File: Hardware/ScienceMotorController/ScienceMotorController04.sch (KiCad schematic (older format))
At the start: 12 parts

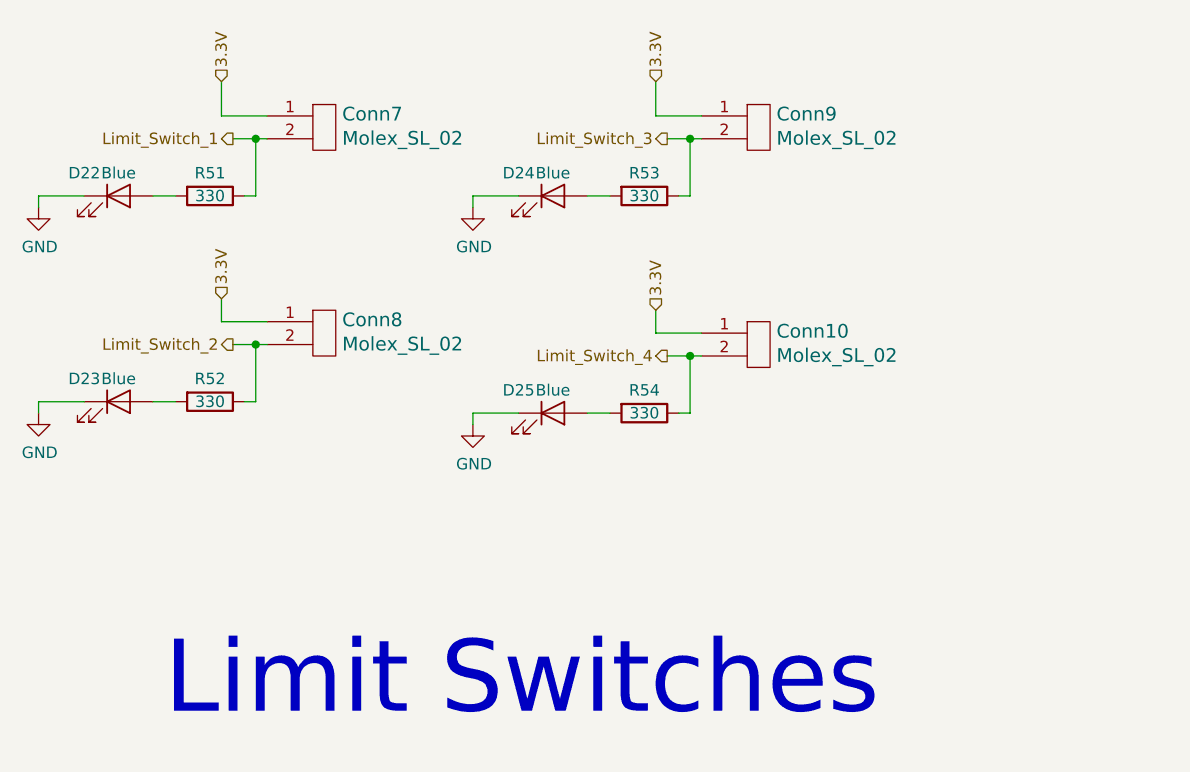
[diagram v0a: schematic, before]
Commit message: assigned most of the footprints
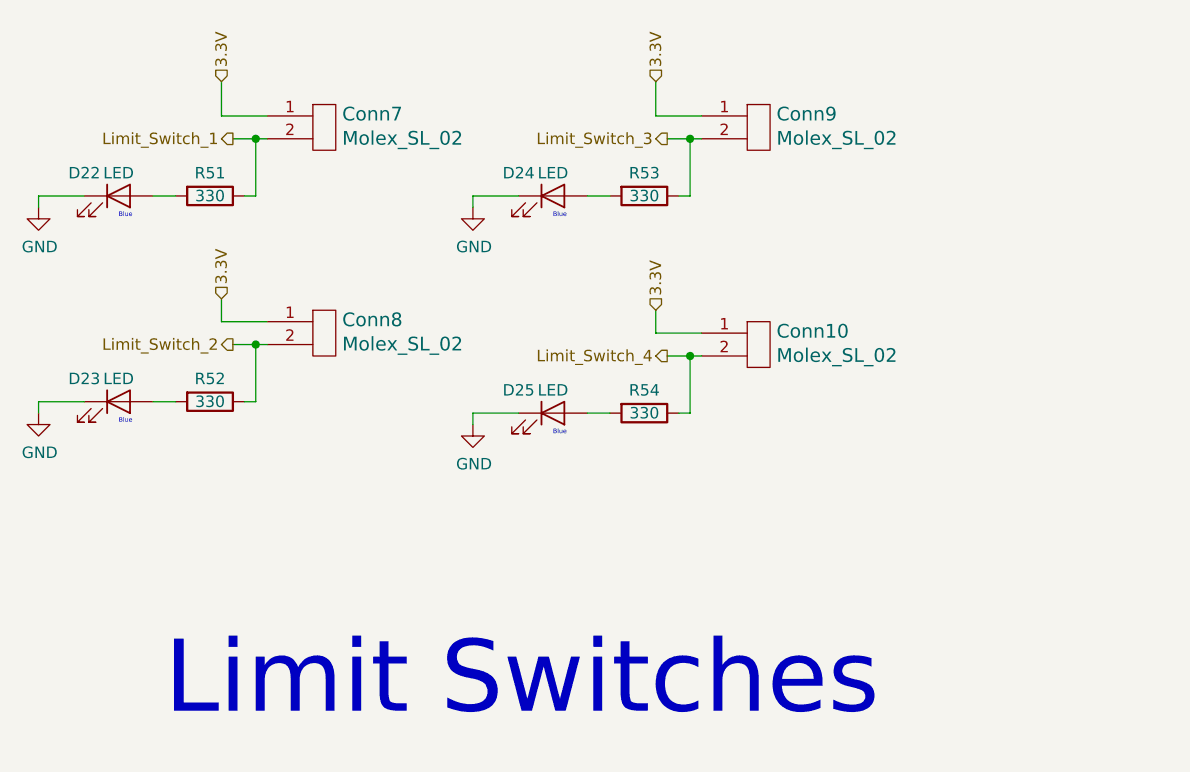
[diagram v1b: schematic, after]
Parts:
- Conn10, Conn7, Conn8, Conn9: footprint (none) -> MRDT_Connectors:MOLEX_SL_02_Vertical
- D22, D23, D24, D25: value Blue -> LED; footprint (none) -> LED_SMD:LED_0603_1608Metric_Pad1.05x0.95mm_HandSolder
- R51, R52, R53, R54: footprint (none) -> Resistor_SMD:R_0603_1608Metric_Pad1.05x0.95mm_HandSolder
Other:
- note added: "Blue"
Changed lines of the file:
@@
 F 0 "Conn7" H 8178 4658 60  0000 L CNN
 F 1 "Molex_SL_02" H 8178 4552 60  0000 L CNN
-F 2 "" H 8050 4400 60  0001 C CNN
+F 2 "MRDT_Connectors:MOLEX_SL_02_Vertical" H 8050 4400 60  0001 C CNN
 F 3 "" H 8050 4400 60  0001 C CNN
 	1    8050 4500
@@
 F 0 "Conn9" H 10078 4658 60  0000 L CNN
 F 1 "Molex_SL_02" H 10078 4552 60  0000 L CNN
-F 2 "" H 9950 4400 60  0001 C CNN
+F 2 "MRDT_Connectors:MOLEX_SL_02_Vertical" H 9950 4400 60  0001 C CNN
 F 3 "" H 9950 4400 60  0001 C CNN
 	1    9950 4500
@@
 F 0 "Conn8" H 8178 5558 60  0000 L CNN
 F 1 "Molex_SL_02" H 8178 5452 60  0000 L CNN
-F 2 "" H 8050 5300 60  0001 C CNN
+F 2 "MRDT_Connectors:MOLEX_SL_02_Vertical" H 8050 5300 60  0001 C CNN
 F 3 "" H 8050 5300 60  0001 C CNN
 	1    8050 5400
@@
 F 0 "Conn10" H 10078 5608 60  0000 L CNN
 F 1 "Molex_SL_02" H 10078 5502 60  0000 L CNN
-F 2 "" H 9950 5350 60  0001 C CNN
+F 2 "MRDT_Connectors:MOLEX_SL_02_Vertical" H 9950 5350 60  0001 C CNN
 F 3 "" H 9950 5350 60  0001 C CNN
 	1    9950 5450
@@
 AR Path="/5F7148FA/5FC42AEE/5FAEAF9B" Ref="D24"  Part="1"
 F 0 "D24" H 8950 4800 50  0000 C CNN
-F 1 "Blue" H 9100 4800 50  0000 C CNN
-F 2 "" H 9100 4700 50  0001 C CNN
+F 1 "LED" H 9100 4800 50  0000 C CNN
+F 2 "LED_SMD:LED_0603_1608Metric_Pad1.05x0.95mm_HandSolder" H 9100 4700 50  0001 C CNN
 F 3 "~" H 9100 4700 50  0001 C CNN
 	1    9100 4700
@@
 AR Path="/5F7148FA/5FC42AEE/5FAEC8F1" Ref="D22"  Part="1"
 F 0 "D22" H 7050 4800 50  0000 C CNN
-F 1 "Blue" H 7200 4800 50  0000 C CNN
-F 2 "" H 7200 4700 50  0001 C CNN
+F 1 "LED" H 7200 4800 50  0000 C CNN
+F 2 "LED_SMD:LED_0603_1608Metric_Pad1.05x0.95mm_HandSolder" H 7200 4700 50  0001 C CNN
 F 3 "~" H 7200 4700 50  0001 C CNN
 	1    7200 4700
@@
 AR Path="/5F7148FA/5FC42AEE/5FAEE0DE" Ref="D23"  Part="1"
 F 0 "D23" H 7050 5700 50  0000 C CNN
-F 1 "Blue" H 7200 5700 50  0000 C CNN
-F 2 "" H 7200 5600 50  0001 C CNN
+F 1 "LED" H 7200 5700 50  0000 C CNN
+F 2 "LED_SMD:LED_0603_1608Metric_Pad1.05x0.95mm_HandSolder" H 7200 5600 50  0001 C CNN
 F 3 "~" H 7200 5600 50  0001 C CNN
 	1    7200 5600
@@
 AR Path="/5F7148FA/5FC42AEE/5FAEEC9D" Ref="D25"  Part="1"
 F 0 "D25" H 8950 5750 50  0000 C CNN
-F 1 "Blue" H 9100 5750 50  0000 C CNN
-F 2 "" H 9100 5650 50  0001 C CNN
+F 1 "LED" H 9100 5750 50  0000 C CNN
+F 2 "LED_SMD:LED_0603_1608Metric_Pad1.05x0.95mm_HandSolder" H 9100 5650 50  0001 C CNN
 F 3 "~" H 9100 5650 50  0001 C CNN
 	1    9100 5650
@@
 F 0 "R53" V 9400 4700 50  0000 C CNN
 F 1 "330" V 9500 4700 50  0000 C CNN
-F 2 "" V 9430 4700 50  0001 C CNN
+F 2 "Resistor_SMD:R_0603_1608Metric_Pad1.05x0.95mm_HandSolder" V 9430 4700 50  0001 C CNN
 F 3 "~" H 9500 4700 50  0001 C CNN
 	1    9500 4700
@@
 F 0 "R51" V 7500 4700 50  0000 C CNN
 F 1 "330" V 7600 4700 50  0000 C CNN
-F 2 "" V 7530 4700 50  0001 C CNN
+F 2 "Resistor_SMD:R_0603_1608Metric_Pad1.05x0.95mm_HandSolder" V 7530 4700 50  0001 C CNN
 F 3 "~" H 7600 4700 50  0001 C CNN
 	1    7600 4700
@@
 F 0 "R54" V 9400 5650 50  0000 C CNN
 F 1 "330" V 9500 5650 50  0000 C CNN
-F 2 "" V 9430 5650 50  0001 C CNN
+F 2 "Resistor_SMD:R_0603_1608Metric_Pad1.05x0.95mm_HandSolder" V 9430 5650 50  0001 C CNN
 F 3 "~" H 9500 5650 50  0001 C CNN
 	1    9500 5650
@@
 F 0 "R52" V 7500 5600 50  0000 C CNN
 F 1 "330" V 7600 5600 50  0000 C CNN
-F 2 "" V 7530 5600 50  0001 C CNN
+F 2 "Resistor_SMD:R_0603_1608Metric_Pad1.05x0.95mm_HandSolder" V 7530 5600 50  0001 C CNN
 F 3 "~" H 7600 5600 50  0001 C CNN
 	1    7600 5600
@@
 Text Notes 7400 7000 0    315  ~ 0
 Limit Switches
+Text Notes 7200 4800 0    20   ~ 0
+Blue
+Text Notes 7200 5700 0    20   ~ 0
+Blue
+Text Notes 9100 5750 0    20   ~ 0
+Blue
+Text Notes 9100 4800 0    20   ~ 0
+Blue
 $EndSCHEMATC

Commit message: running traces
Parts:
- renumbered Conn9 to Conn10, Conn10 to Conn11, Conn7 to Conn8, Conn8 to Conn9
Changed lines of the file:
@@
 P 8050 4500
 AR Path="/5F81B171/5F81B312" Ref="Conn?"  Part="1"
-AR Path="/5F7148FA/5FC42AEE/5F81B312" Ref="Conn7"  Part="1"
-F 0 "Conn7" H 8178 4658 60  0000 L CNN
+AR Path="/5F7148FA/5FC42AEE/5F81B312" Ref="Conn8"  Part="1"
+F 0 "Conn8" H 8178 4658 60  0000 L CNN
 F 1 "Molex_SL_02" H 8178 4552 60  0000 L CNN
 F 2 "MRDT_Connectors:MOLEX_SL_02_Vertical" H 8050 4400 60  0001 C CNN
@@
 P 9950 4500
 AR Path="/5F81B171/5F81C1D4" Ref="Conn?"  Part="1"
-AR Path="/5F7148FA/5FC42AEE/5F81C1D4" Ref="Conn9"  Part="1"
-F 0 "Conn9" H 10078 4658 60  0000 L CNN
+AR Path="/5F7148FA/5FC42AEE/5F81C1D4" Ref="Conn10"  Part="1"
+F 0 "Conn10" H 10078 4658 60  0000 L CNN
 F 1 "Molex_SL_02" H 10078 4552 60  0000 L CNN
 F 2 "MRDT_Connectors:MOLEX_SL_02_Vertical" H 9950 4400 60  0001 C CNN
@@
 P 8050 5400
 AR Path="/5F81B171/5F81C7E8" Ref="Conn?"  Part="1"
-AR Path="/5F7148FA/5FC42AEE/5F81C7E8" Ref="Conn8"  Part="1"
-F 0 "Conn8" H 8178 5558 60  0000 L CNN
+AR Path="/5F7148FA/5FC42AEE/5F81C7E8" Ref="Conn9"  Part="1"
+F 0 "Conn9" H 8178 5558 60  0000 L CNN
 F 1 "Molex_SL_02" H 8178 5452 60  0000 L CNN
 F 2 "MRDT_Connectors:MOLEX_SL_02_Vertical" H 8050 5300 60  0001 C CNN
@@
 P 9950 5450
 AR Path="/5F81B171/5F81D13D" Ref="Conn?"  Part="1"
-AR Path="/5F7148FA/5FC42AEE/5F81D13D" Ref="Conn10"  Part="1"
-F 0 "Conn10" H 10078 5608 60  0000 L CNN
+AR Path="/5F7148FA/5FC42AEE/5F81D13D" Ref="Conn11"  Part="1"
+F 0 "Conn11" H 10078 5608 60  0000 L CNN
 F 1 "Molex_SL_02" H 10078 5502 60  0000 L CNN
 F 2 "MRDT_Connectors:MOLEX_SL_02_Vertical" H 9950 5350 60  0001 C CNN
